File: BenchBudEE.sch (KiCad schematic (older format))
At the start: 0 parts

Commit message: Fan Module details
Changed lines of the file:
@@
 F3 "Power-" I R 8600 1400 60
 F4 "Tach" I R 8600 1700 60
-F5 "Tach_out" O L 7100 1250 60
+F5 "Tach_out" O L 7100 2200 60
 F6 "Fan_In" I L 7100 1050 60
+F7 "Current_Measure" O L 7100 2000 60
+F8 "MOSI" I L 7100 1200 60
+F9 "MISO" O L 7100 1400 60
+F10 "CS_N" I L 7100 1600 60
+F11 "SCLK" I L 7100 1800 60
 $EndSheet
 $Sheet

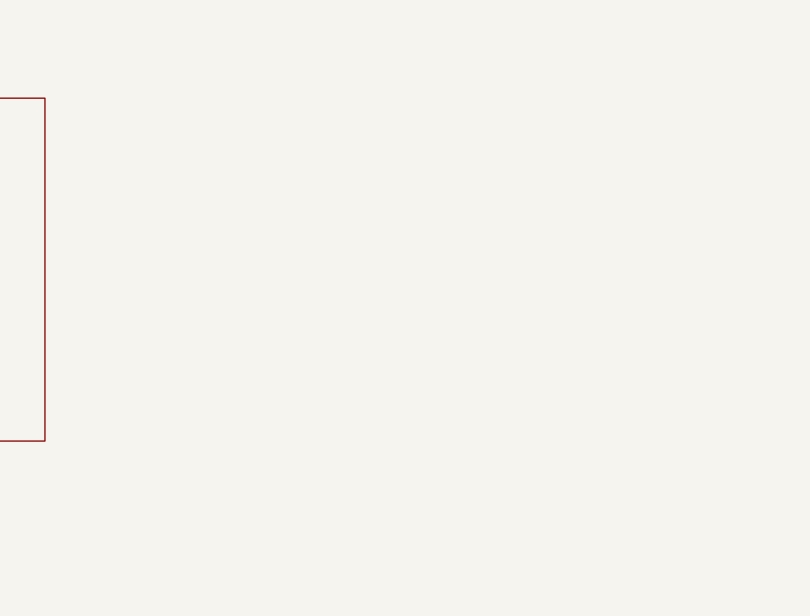
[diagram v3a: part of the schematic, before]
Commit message: Power Protection & Filtering
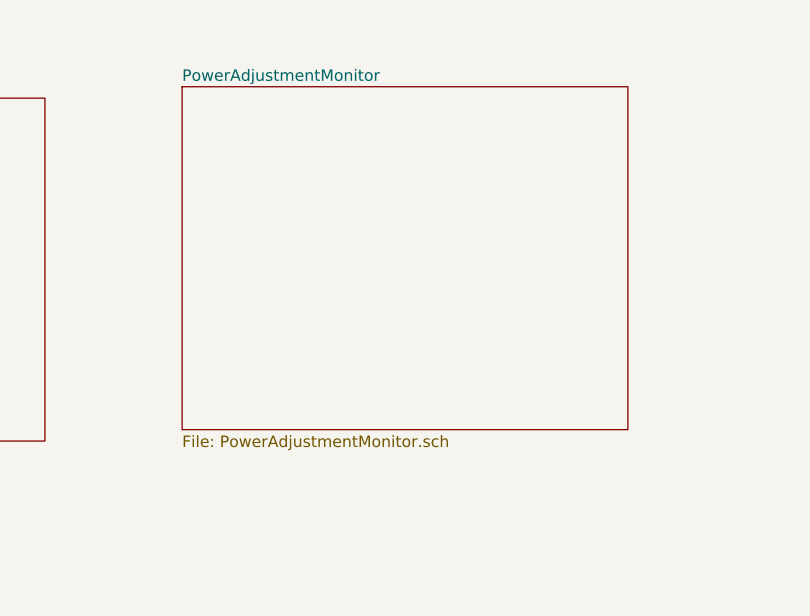
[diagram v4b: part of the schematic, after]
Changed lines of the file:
@@
 $Descr A4 11693 8268
 encoding utf-8
-Sheet 1 8
+Sheet 1 9
 Title ""
-Date "21 may 2014"
+Date "22 may 2014"
 Rev ""
 Comp ""
@@
 F5 "Relay-" O R 8700 6150 60
 $EndSheet
+$Sheet
+S 3900 900  1950 1500
+U 537D725F
+F0 "PowerAdjustmentMonitor" 50
+F1 "PowerAdjustmentMonitor.sch" 50
+$EndSheet
 $EndSCHEMATC
